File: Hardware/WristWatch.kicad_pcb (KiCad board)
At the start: 2 copper layers, 32 x 32 mm, 100 parts, among them J1 vcc, J2 gnd, J3 vcc, J4 gnd, Q1 Q_PMOS_GSD, U3 LIS2DE12, U4 AP2205-3.0, U5 MCP73832-2-OT, U6 ESP32-C3, Y2 40M, Y3 32.768k

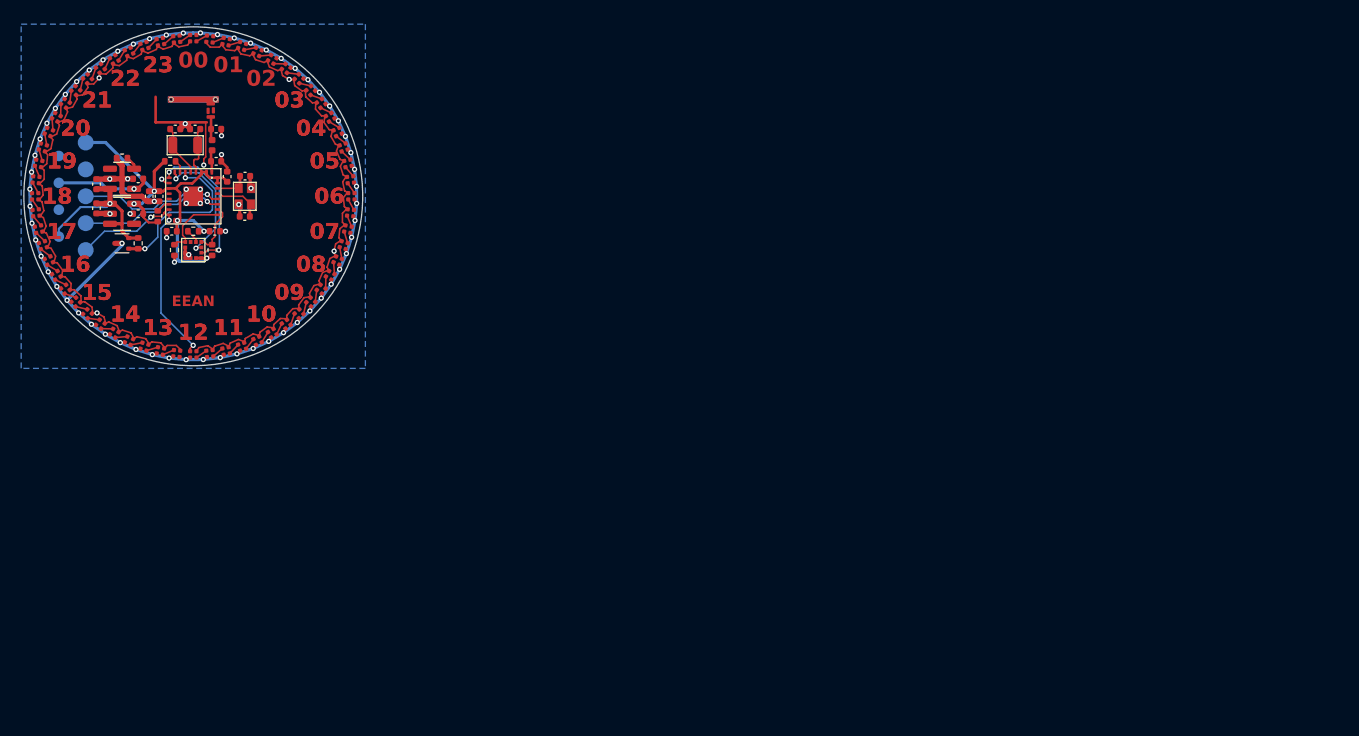
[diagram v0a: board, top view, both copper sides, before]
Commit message: rev C for shift registered discrete 0603 LEDs
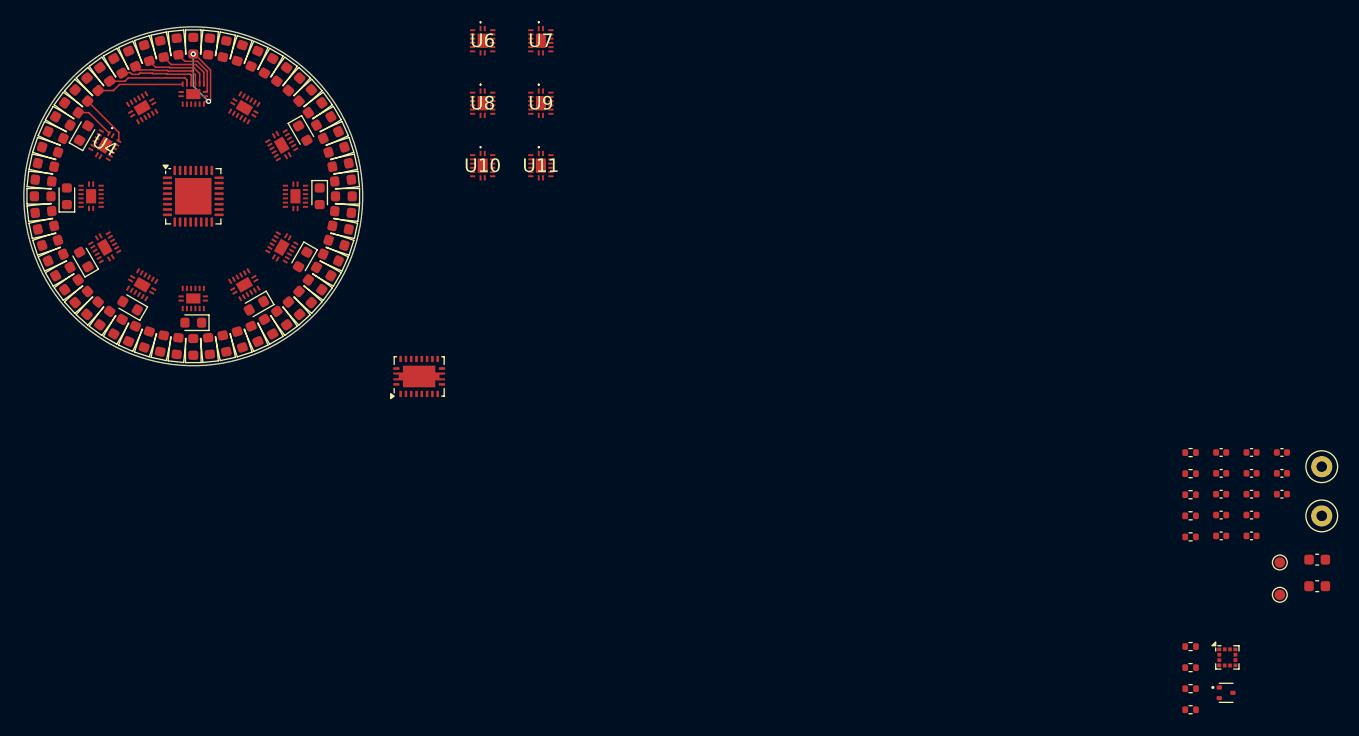
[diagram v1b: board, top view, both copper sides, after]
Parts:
- removed AE1: Antenna_Shield, Antenna_SMD:C209892
- removed C12: 1u, Capacitor_SMD:C_0402_1005Metric
- removed C13: 2u2, Capacitor_SMD:C_0402_1005Metric
- removed C15: 4u7, Capacitor_SMD:C_0402_1005Metric
- removed the C21 at (-2.03, 3.30)
- removed the C21 at (2.03, 3.30)
- removed J1, J3: vcc, TestPoint:TestPoint_Pad_D1.0mm
- removed J2, J4: gnd, TestPoint:TestPoint_Pad_D1.0mm
- removed L2: 3n, Inductor_SMD:L_0402_1005Metric
- removed TP3: BOOT, TestPoint:TestPoint_Pad_D1.5mm
- removed TP5: VCC, TestPoint:TestPoint_Pad_D1.5mm
- removed TP6: GND, TestPoint:TestPoint_Pad_D1.5mm
- removed Y2: 40M, Crystal:Crystal_SMD_2520-4Pin_2.5x2.0mm
- removed Y3: 32.768k, Crystal:Crystal_SMD_EuroQuartz_EQ161-2Pin_3.2x1.5mm
- added C2: 47n, Capacitor_SMD:C_0402_1005Metric, F.Cu at (97.1, 26.2)
- added C21: 10n, Capacitor_SMD:C_0402_1005Metric, F.Cu at (100.0, 32.1)
- added C23: 470n, Capacitor_SMD:C_0402_1005Metric, F.Cu at (102.8, 26.2)
- added C24: 22n, Capacitor_SMD:C_0402_1005Metric, F.Cu at (102.8, 28.1)
- added C25: 4.7u, Capacitor_SMD:C_0603_1608Metric, F.Cu at (106.2, 36.8)
- added D63: LED_Small, LED_SMD:LED_0603_1608Metric, F.Cu at (-10.3, -5.97)
- added D64: LED_Small, LED_SMD:LED_0603_1608Metric, F.Cu at (-11.9, 0.00)
- added D65: LED_Small, LED_SMD:LED_0603_1608Metric, F.Cu at (-10.3, 5.97)
- added D66: LED_Small, LED_SMD:LED_0603_1608Metric, F.Cu at (-5.97, 10.3)
- added D67: LED_Small, LED_SMD:LED_0603_1608Metric, F.Cu at (0.00, 11.9)
- added D68: LED_Small, LED_SMD:LED_0603_1608Metric, F.Cu at (5.97, 10.3)
- added D69: LED_Small, LED_SMD:LED_0603_1608Metric, F.Cu at (10.3, 5.97)
- added D70: LED_Small, LED_SMD:LED_0603_1608Metric, F.Cu at (11.9, 0.00)
- added D71: LED_Small, LED_SMD:LED_0603_1608Metric, F.Cu at (10.3, -5.97)
- added J5: vcc, TestPoint:TestPoint_Pad_D1.0mm, F.Cu at (102.6, 34.6)
- added J6: gnd, TestPoint:TestPoint_Pad_D1.0mm, F.Cu at (102.6, 37.6)
- added R11: 3k, Resistor_SMD:R_0402_1005Metric, F.Cu at (94.2, 28.2)
- added R13: 20K, Resistor_SMD:R_0402_1005Metric, F.Cu at (94.2, 32.2)
- added U1: 74HC595, KiCad:74HC595BZX, F.Cu at (4.83, -8.36)
- added U10: 74HC595, KiCad:74HC595BZX, F.Cu at (27.3, -2.89)
- added U11: 74HC595, KiCad:74HC595BZX, F.Cu at (32.8, -2.89)
- added U12: 74HC595, KiCad:74HC595BZX, F.Cu at (0.00, -9.65)
- added U13: 74HC595, KiCad:74HC595BZX, F.Cu at (-4.83, -8.36)
- added U15: 74HC595, KiCad:74HC595BZX, F.Cu at (-9.65, 0.00)
- added U16: 74HC595, KiCad:74HC595BZX, F.Cu at (-8.36, 4.83)
- added U17: 74HC595, KiCad:74HC595BZX, F.Cu at (-4.83, 8.36)
- added U18: 74HC595, KiCad:74HC595BZX, F.Cu at (0.00, 9.65)
- added U19: 74HC595, KiCad:74HC595BZX, F.Cu at (4.83, 8.36)
- added U2: STM32L412KBUx, Package_DFN_QFN:QFN-32-1EP_5x5mm_P0.5mm_EP3.45x3.45mm, F.Cu at (0.00, 0.00)
- added U20: 74HC595, KiCad:74HC595BZX, F.Cu at (8.36, 4.83)
- added U21: 74HC595, KiCad:74HC595BZX, F.Cu at (9.65, 0.00)
- added U22: 74HC595, KiCad:74HC595BZX, F.Cu at (8.36, -4.83)
- added U7: 74HC595, KiCad:74HC595BZX, F.Cu at (32.8, -14.7)
- added U8: 74HC595, KiCad:74HC595BZX, F.Cu at (27.3, -8.79)
- added U9: 74HC595, KiCad:74HC595BZX, F.Cu at (32.8, -8.79)
- C1: value 12p -> 68n
- C14: value 4u7 -> 100p
- C16: value 12p -> 470n
- C17: value 10u -> 100n
- C18: value 1.2p -> 4.7u; footprint Capacitor_SMD:C_0402_1005Metric -> Capacitor_SMD:C_0603_1608Metric
- C19: value 1.8p -> 22n
- C20: value 100n -> 10n
- C22: value 100n -> 22n
- C4: value 12p -> 39n
- C7: value 12p -> 2.2n
- D1, D10, D11, D12, D13, D14, D15, D16, D17, D18, D19, D2, D20, D21, D22, D23, D24, D25, D26, D27, D28, D29, D3, D30, D31, D32, D33, D34, D35, D36, D37, D38, D39, D4, D40, D41, D42, D43, D44, D45, D46, D47, D48, D49, D5, D50, D51, D52, D53, D54, D55, D56, D57, D58, D59, D6, D60, D7, D8, D9: value WS2812B -> LED_Small; footprint LED_Custom:XL-1010RGBC -> LED_SMD:LED_0603_1608Metric
- R1: value 100k -> 10K
- R10: value 10k -> 2.43K
- R12: value 100k -> 200
- TP1: value TX -> TestPoint; footprint TestPoint:TestPoint_Pad_D1.5mm -> TestPoint:TestPoint_Loop_D1.80mm_Drill1.0mm_Beaded; moved to F.Cu
- TP2: value RX -> TestPoint; footprint TestPoint:TestPoint_Pad_D1.5mm -> TestPoint:TestPoint_Loop_D1.80mm_Drill1.0mm_Beaded; moved to F.Cu
- U4: value AP2205-3.0 -> 74HC595; footprint Package_TO_SOT_SMD:SOT-23-5 -> KiCad:74HC595BZX
- U5: value MCP73832-2-OT -> BQ51050BRHL; footprint Package_TO_SOT_SMD:SOT-23-5 -> Package_DFN_QFN:Texas_VQFN-RHL-20
- U6: value ESP32-C3 -> 74HC595; footprint Package_DFN_QFN:QFN-32-1EP_5x5mm_P0.5mm_EP3.7x3.7mm -> KiCad:74HC595BZX
- moved TP2 120.0 mm to (106.6, 30.2)
- moved TP1 119.5 mm to (106.6, 25.5)
- moved Q1 112.6 mm to (97.6, 46.9), turned to 0 degrees
- moved C18 110.6 mm to (106.2, 34.3)
- moved C22 108.8 mm to (102.8, 24.2), turned to 0 degrees
- moved C14 107.7 mm to (97.1, 32.1), turned to 0 degrees
- moved C17 107.4 mm to (100.0, 26.2), turned to 0 degrees
- moved R6 106.5 mm to (94.2, 42.5), turned to 0 degrees
- moved R10 105.2 mm to (94.2, 26.2)
- moved U3 105.0 mm to (97.7, 43.6), turned to 0 degrees
- moved C4 104.6 mm to (97.1, 28.1), turned to 0 degrees
- moved R8 104.5 mm to (94.2, 46.5), turned to 0 degrees
- moved R9 104.5 mm to (94.2, 48.5), turned to 0 degrees
- moved C19 103.7 mm to (100.0, 28.1)
- moved R12 102.0 mm to (94.2, 30.2), turned to 0 degrees
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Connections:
- C1 pad 1: GND -> Net-(C1-Pad1)
- C1 pad 2: /xtl_ls+ -> /BMS/Coil+
- C14 pad 1: VBUS -> /BMS/Coil-
- C14 pad 2: GND -> /BMS/Coil+
- C16 pad 1: GND -> /BMS/Coil+
- C16 pad 2: /xtl_hs- -> Net-(U5-CLAMP1)
- C17 pad 1: +3V0 -> GND
- C17 pad 2: GND -> +BATT
- C18 pad 1: Net-(U6-LNA_IN) -> GND
- C18 pad 2: GND -> +BATT
- C19 pad 1: Net-(AE1-A) -> /BMS/Coil+
- C19 pad 2: GND -> Net-(U5-COMM1)
- C20 pad 1: GND -> /BMS/Coil+
- C20 pad 2: +3V0 -> Net-(U5-BOOT1)
- C22 pad 1: GND -> /BMS/Coil-
- C22 pad 2: +3V0 -> Net-(U5-COMM2)
- C4 pad 1: GND -> Net-(C1-Pad1)
- C4 pad 2: /xtl_ls- -> /BMS/Coil+
- C7 pad 1: GND -> /BMS/Coil-
- C7 pad 2: /xtl_hs+ -> /BMS/Coil+
- D1 pad 1: VLED -> /LED Array/LED_OUT
- D1 pad 2: Net-(D1-DOUT) -> Net-(D1-A)
- D10 pad 1: VLED -> /LED Array/LED_OUT
- D10 pad 2: Net-(D10-DOUT) -> Net-(D10-A)
- D11 pad 1: VLED -> /LED Array/LED_OUT
- D11 pad 2: Net-(D11-DOUT) -> Net-(D11-A)
- D12 pad 1: VLED -> /LED Array/LED_OUT
- D12 pad 2: Net-(D12-DOUT) -> Net-(D12-A)
- D13 pad 1: VLED -> /LED Array/LED_OUT
- D13 pad 2: Net-(D13-DOUT) -> Net-(D13-A)
- D14 pad 1: VLED -> /LED Array/LED_OUT
- D14 pad 2: Net-(D14-DOUT) -> Net-(D14-A)
- D15 pad 1: VLED -> /LED Array/LED_OUT
- D15 pad 2: Bank2 -> Net-(D15-A)
- D16 pad 1: VLED -> /LED Array/LED_OUT
- D16 pad 2: Net-(D16-DOUT) -> Net-(D16-A)
- D17 pad 1: VLED -> /LED Array/LED_OUT
- D17 pad 2: Net-(D17-DOUT) -> Net-(D17-A)
- D18 pad 1: VLED -> /LED Array/LED_OUT
- D18 pad 2: Net-(D18-DOUT) -> Net-(D18-A)
- D19 pad 1: VLED -> /LED Array/LED_OUT
- D19 pad 2: Net-(D19-DOUT) -> Net-(D19-A)
- D2 pad 1: VLED -> /LED Array/LED_OUT
- D2 pad 2: Net-(D2-DOUT) -> Net-(D2-A)
- D20 pad 1: VLED -> /LED Array/LED_OUT
- D20 pad 2: Net-(D20-DOUT) -> Net-(D20-A)
- D21 pad 1: VLED -> /LED Array/LED_OUT
- D21 pad 2: Net-(D21-DOUT) -> Net-(D21-A)
- D22 pad 1: VLED -> /LED Array/LED_OUT
- D22 pad 2: Net-(D22-DOUT) -> Net-(D22-A)
- D23 pad 1: VLED -> /LED Array/LED_OUT
- D23 pad 2: Net-(D23-DOUT) -> Net-(D23-A)
- D24 pad 1: VLED -> /LED Array/LED_OUT
- D24 pad 2: Net-(D24-DOUT) -> Net-(D24-A)
- D25 pad 1: VLED -> /LED Array/LED_OUT
- D25 pad 2: Net-(D25-DOUT) -> Net-(D25-A)
- D26 pad 1: VLED -> /LED Array/LED_OUT
- D26 pad 2: Net-(D26-DOUT) -> Net-(D26-A)
- D27 pad 1: VLED -> /LED Array/LED_OUT
- D27 pad 2: Net-(D27-DOUT) -> Net-(D27-A)
- D28 pad 1: VLED -> /LED Array/LED_OUT
- D28 pad 2: Net-(D28-DOUT) -> Net-(D28-A)
- D29 pad 1: VLED -> /LED Array/LED_OUT
- D29 pad 2: Net-(D29-DOUT) -> Net-(D29-A)
- D3 pad 1: VLED -> /LED Array/LED_OUT
- D3 pad 2: Net-(D3-DOUT) -> Net-(D3-A)
- D30 pad 1: VLED -> /LED Array/LED_OUT
- D30 pad 2: unconnected-(D30-DOUT-Pad2) -> Net-(D30-A)
- D31 pad 1: VLED -> /LED Array/LED_OUT
- D31 pad 2: Net-(D31-DOUT) -> Net-(D31-A)
- D32 pad 1: VLED -> /LED Array/LED_OUT
- D32 pad 2: Net-(D32-DOUT) -> Net-(D32-A)
- D33 pad 1: VLED -> /LED Array/LED_OUT
- D33 pad 2: Net-(D33-DOUT) -> Net-(D33-A)
- D34 pad 1: VLED -> /LED Array/LED_OUT
- D34 pad 2: Net-(D34-DOUT) -> Net-(D34-A)
- D35 pad 1: VLED -> /LED Array/LED_OUT
- D35 pad 2: Net-(D35-DOUT) -> Net-(D35-A)
- D36 pad 1: VLED -> /LED Array/LED_OUT
- D36 pad 2: Net-(D36-DOUT) -> Net-(D36-A)
- D37 pad 1: VLED -> /LED Array/LED_OUT
- D37 pad 2: Net-(D37-DOUT) -> Net-(D37-A)
- D38 pad 1: VLED -> /LED Array/LED_OUT
- D38 pad 2: Net-(D38-DOUT) -> Net-(D38-A)
- D39 pad 1: VLED -> /LED Array/LED_OUT
- D39 pad 2: Net-(D39-DOUT) -> Net-(D39-A)
- D4 pad 1: VLED -> /LED Array/LED_OUT
- D4 pad 2: Net-(D4-DOUT) -> Net-(D4-A)
- D40 pad 1: VLED -> /LED Array/LED_OUT
- D40 pad 2: Net-(D40-DOUT) -> Net-(D40-A)
- D41 pad 1: VLED -> /LED Array/LED_OUT
- D41 pad 2: Net-(D41-DOUT) -> Net-(D41-A)
- D42 pad 1: VLED -> /LED Array/LED_OUT
- D42 pad 2: Net-(D42-DOUT) -> Net-(D42-A)
- D43 pad 1: VLED -> /LED Array/LED_OUT
- D43 pad 2: Net-(D43-DOUT) -> Net-(D43-A)
- D44 pad 1: VLED -> /LED Array/LED_OUT
- D44 pad 2: Net-(D44-DOUT) -> Net-(D44-A)
- D45 pad 1: VLED -> /LED Array/LED_OUT
- D45 pad 2: Bank3 -> Net-(D45-A)
- D46 pad 1: VLED -> /LED Array/LED_OUT
- D46 pad 2: Net-(D46-DOUT) -> Net-(D46-A)
- D47 pad 1: VLED -> /LED Array/LED_OUT
- D47 pad 2: Net-(D47-DOUT) -> Net-(D47-A)
- D48 pad 1: VLED -> /LED Array/LED_OUT
- D48 pad 2: Net-(D48-DOUT) -> Net-(D48-A)
- D49 pad 1: VLED -> /LED Array/LED_OUT
- D49 pad 2: Net-(D49-DOUT) -> Net-(D49-A)
- D5 pad 1: VLED -> /LED Array/LED_OUT
- D5 pad 2: Net-(D5-DOUT) -> Net-(D5-A)
- D50 pad 1: VLED -> /LED Array/LED_OUT
- D50 pad 2: Net-(D50-DOUT) -> Net-(D50-A)
- D51 pad 1: VLED -> /LED Array/LED_OUT
- D51 pad 2: Net-(D51-DOUT) -> Net-(D51-A)
- D52 pad 1: VLED -> /LED Array/LED_OUT
- D52 pad 2: Net-(D52-DOUT) -> Net-(D52-A)
- D53 pad 1: VLED -> /LED Array/LED_OUT
- D53 pad 2: Net-(D53-DOUT) -> Net-(D53-A)
- D54 pad 1: VLED -> /LED Array/LED_OUT
- D54 pad 2: Net-(D54-DOUT) -> Net-(D54-A)
- D55 pad 1: VLED -> /LED Array/LED_OUT
- D55 pad 2: Net-(D55-DOUT) -> Net-(D55-A)
- D56 pad 1: VLED -> /LED Array/LED_OUT
- D56 pad 2: Net-(D56-DOUT) -> Net-(D56-A)
- D57 pad 1: VLED -> /LED Array/LED_OUT
- D57 pad 2: Net-(D57-DOUT) -> Net-(D57-A)
- D58 pad 1: VLED -> /LED Array/LED_OUT
- D58 pad 2: Net-(D58-DOUT) -> Net-(D58-A)
- D59 pad 1: VLED -> /LED Array/LED_OUT
- D59 pad 2: Net-(D59-DOUT) -> Net-(D59-A)
- D6 pad 1: VLED -> /LED Array/LED_OUT
- D6 pad 2: Net-(D6-DOUT) -> Net-(D6-A)
- D60 pad 1: VLED -> /LED Array/LED_OUT
- D60 pad 2: Bank1 -> Net-(D100-A)
- D7 pad 1: VLED -> /LED Array/LED_OUT
- D7 pad 2: Net-(D7-DOUT) -> Net-(D7-A)
- D8 pad 1: VLED -> /LED Array/LED_OUT
- D8 pad 2: Net-(D8-DOUT) -> Net-(D8-A)
- D9 pad 1: VLED -> /LED Array/LED_OUT
- D9 pad 2: Net-(D10-DIN) -> Net-(D9-A)
- R1 pad 1: Net-(U6-GPIO8) -> Net-(U5-TS/CTRL)
- R1 pad 2: +3V0 -> GND
- R10 pad 1: GND -> Net-(U5-TERM)
- R10 pad 2: Net-(U5-PROG) -> GND
- R12 pad 1: Net-(U6-CHIP_EN) -> FOD
- R12 pad 2: +3V0 -> GND
- TP1 pad 1: ESP_TX -> Net-(C1-Pad1)
- TP2 pad 1: ESP_RX -> /BMS/Coil-
- U4 pad 1: +BATT -> Net-(D10-A)
- U4 pad 2: GND -> Net-(D11-A)
- U4 pad 3: +BATT -> Net-(D12-A)
- U4 pad 4: unconnected-(U4-NC-Pad4) -> Net-(D13-A)
- U4 pad 5: +3V0 -> Net-(D14-A)
- U5 pad 1: BMS_STATUS -> GND
- U5 pad 2: GND -> /BMS/Coil+
- U5 pad 3: +BATT -> Net-(U5-BOOT1)
- U5 pad 4: VBUS -> +BATT
- U5 pad 5: Net-(U5-PROG) -> Net-(U5-CLAMP1)
- U6 pad 1: Net-(U6-LNA_IN) -> Net-(D18-A)
- U6 pad 10: unconnected-(U6-MTDI-Pad10) -> /LED Array/SR_CLEAR_IN
- U6 pad 11: +3V0 -> /LED Array/SR_SERIAL_IN
- U6 pad 12: unconnected-(U6-MTCK-Pad12) -> /LED Array/SR_LATCH_IN
- U6 pad 13: BMS_STATUS -> /LED Array/SR_OE_IN
- U6 pad 14: Net-(U6-GPIO8) -> Net-(U4-QH')
- U6 pad 15: ESP_BOOT -> Net-(D17-A)
- U6 pad 16: LED_DATA -> VLED
- U6 pad 17: +3V0 -> (no net)
- U6 pad 2: +3V0 -> Net-(D19-A)
- U6 pad 3: +3V0 -> Net-(D20-A)
- U6 pad 4: /xtl_ls+ -> Net-(D21-A)
- U6 pad 5: /xtl_ls- -> Net-(D22-A)
- U6 pad 6: LED_PWR_EN -> Net-(D23-A)
- U6 pad 7: Net-(U6-CHIP_EN) -> Net-(D24-A)
- U6 pad 8: IMU_MOVE_INT -> GND
- U6 pad 9: IMU_SPAR_INT -> Net-(U6-QH')
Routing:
- net GND: track 146.1 -> 0.00 mm, vias 22 -> 0
- net VLED: track 130.7 -> 0.00 mm, vias 61 -> 0
- net +3V0: track 46.8 -> 0.00 mm, vias 6 -> 0
- net +BATT: track 17.1 -> 0.00 mm, vias 1 -> 0
- net LED_PWR_EN: track 15.6 -> 0.00 mm, vias 2 -> 0
- net LED_DATA: track 14.6 -> 0.00 mm, vias 2 -> 0
- net IMU_SPAR_INT: track 13.9 -> 0.00 mm, vias 2 -> 0
- net ESP_TX: track 13.7 -> 0.00 mm, vias 1 -> 0
- net ESP_RX: track 13.7 -> 0.00 mm, vias 1 -> 0
- net IMU_MOVE_INT: track 12.2 -> 0.00 mm, vias 2 -> 0
- net Net-(D1-A): track 0.00 -> 11.0 mm, vias 0 -> 2
- net ESP_BOOT: track 9.52 -> 0.00 mm, vias 1 -> 0
- net VBUS: track 8.86 -> 0.00 mm, vias 1 -> 0
- net Net-(D8-A): track 0.00 -> 8.25 mm
- net Net-(D7-A): track 0.00 -> 7.90 mm
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- removed copper zone on B.Cu, net GND
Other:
- board text removed: "00"
- board text removed: "01"
- board text removed: "02"
- board text removed: "03"
- board text removed: "04"
- board text removed: "05"
- board text removed: "06"
- board text removed: "07"
- board text removed: "08"
- board text removed: "09"
- board text removed: "10"
- board text removed: "11"
- board text removed: "12"
- board text removed: "13"
- board text removed: "14"
- board text removed: "15"
- board text removed: "16"
- board text removed: "17"
- board text removed: "18"
- board text removed: "19"
- board text removed: "20"
- board text removed: "21"
- board text removed: "22"
- board text removed: "23"
- board text removed: "EEAN"

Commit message: semi-final component placements and final component selections. Abandoning due to high routing complexity and need for a 4L board.
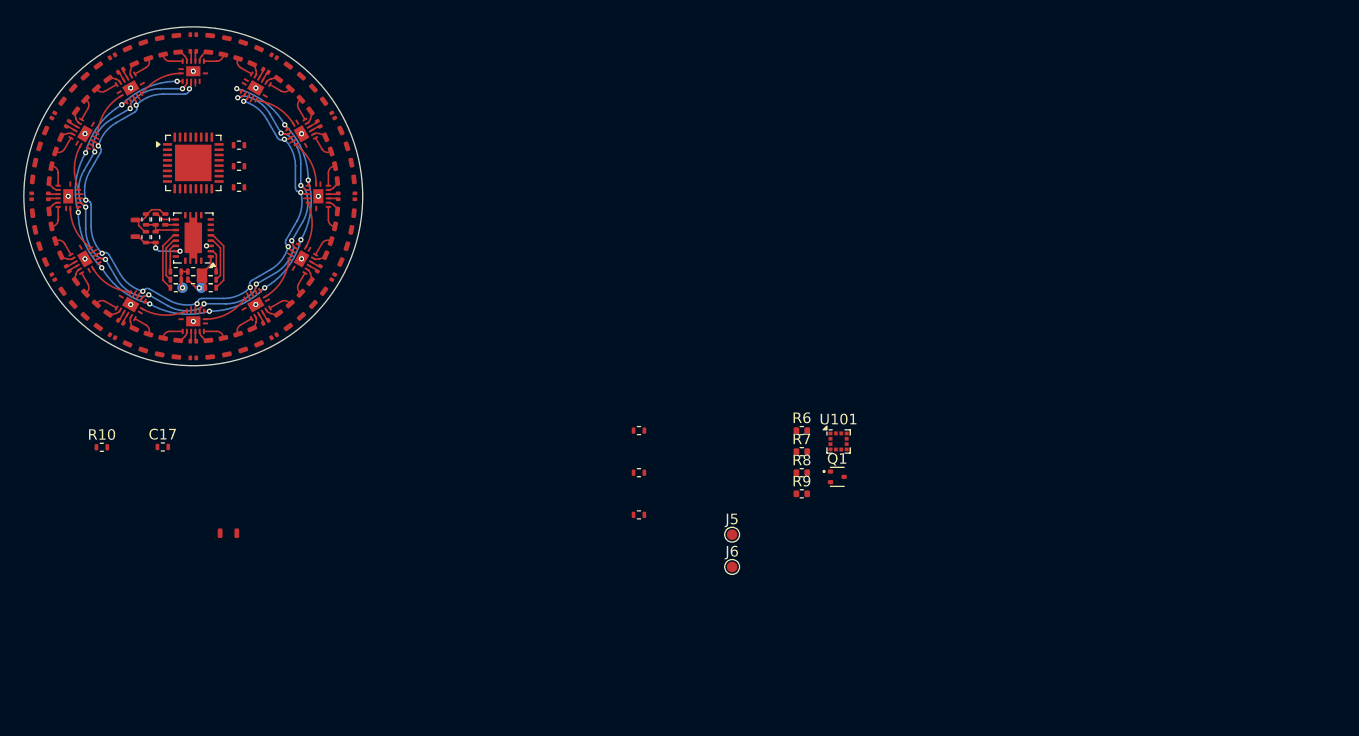
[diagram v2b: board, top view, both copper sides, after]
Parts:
- removed D63, D64, D65, D66, D67, D68, D69, D70, D71: LED_Small, LED_SMD:LED_0603_1608Metric
- removed U13, U15, U16, U17, U18, U19, U20, U21, U22: 74HC595, KiCad:74HC595BZX
- added C3: 100n, LED_Custom:SMD_0402-2, F.Cu at (4.32, -4.83)
- added C5: 100n, LED_Custom:SMD_0402-2, F.Cu at (4.32, -2.84)
- added C6: 100n, LED_Custom:SMD_0402-2, F.Cu at (4.32, -0.85)
- added U100: STM32L412KBUx, Package_DFN_QFN:QFN-32-1EP_5x5mm_P0.5mm_EP3.45x3.45mm, F.Cu at (0.00, -3.15)
- added U101: LIS2DE12, Package_LGA:LGA-12_2x2mm_P0.5mm, F.Cu at (61.0, 23.2)
- added U102: BQ51050BRHL, Package_DFN_QFN:Texas_VQFN-RHL-20, F.Cu at (0.00, 3.94)
- C1, C14, C16, C17, C19, C20, C21, C22, C23, C24, C4, C7: footprint Capacitor_SMD:C_0402_1005Metric -> LED_Custom:SMD_0402-2
- C18, C25: footprint Capacitor_SMD:C_0603_1608Metric -> LED_Custom:LED_0603-2
- C2: value 47n -> 220n; footprint Capacitor_SMD:C_0402_1005Metric -> LED_Custom:SMD_0402-2
- D1, D10, D11, D12, D14, D15, D16, D17, D19, D2, D20, D21, D22, D24, D25, D26, D27, D29, D30, D31, D32, D34, D35, D36, D37, D39, D4, D40, D41, D42, D44, D45, D46, D47, D49, D5, D50, D51, D52, D54, D55, D56, D57, D59, D6, D60, D7, D9: footprint LED_SMD:LED_0603_1608Metric -> LED_Custom:LED_0603-2
- D13, D18, D23, D28, D3, D33, D38, D43, D48, D53, D58, D8: footprint LED_SMD:LED_0603_1608Metric -> LED_Custom:LED_0603-4
- R1, R10, R11, R12, R13: footprint Resistor_SMD:R_0402_1005Metric -> LED_Custom:SMD_0402-2
- TP1, TP2: footprint TestPoint:TestPoint_Loop_D1.80mm_Drill1.0mm_Beaded -> TestPoint:TestPoint_Pad_D1.0mm; moved to B.Cu
- U1: value 74HC595 -> 74HC595BZX
- U2: value STM32L412KBUx -> 74HC595; footprint Package_DFN_QFN:QFN-32-1EP_5x5mm_P0.5mm_EP3.45x3.45mm -> KiCad:74HC595BZX
- U3: value LIS2DE12 -> 74HC595; footprint Package_LGA:LGA-12_2x2mm_P0.5mm -> KiCad:74HC595BZX
- U5: value BQ51050BRHL -> 74HC595; footprint Package_DFN_QFN:Texas_VQFN-RHL-20 -> KiCad:74HC595BZX
- moved U3 118.7 mm to (-10.2, -5.91), turned to -30 degrees
- moved C25 116.6 mm to (-5.46, 3.02), turned to -90 degrees
- moved C24 110.0 mm to (-4.47, 3.86), turned to -90 degrees
- moved TP2 109.7 mm to (-1.02, 8.64)
- moved TP1 107.2 mm to (0.76, 8.64)
- moved C23 106.1 mm to (-1.65, 7.87), turned to 180 degrees
- moved C22 105.6 mm to (-1.65, 8.64), turned to 180 degrees
- moved C21 104.6 mm to (-1.65, 7.11), turned to 180 degrees
- moved C18 102.9 mm to (3.33, 31.8)
- moved C17 102.9 mm to (-2.87, 23.7)
- moved R10 102.9 mm to (-8.63, 23.7)
- moved R12 102.6 mm to (-4.47, 2.18), turned to 90 degrees
- moved R13 101.8 mm to (-3.56, 3.86), turned to -90 degrees
- moved R11 101.2 mm to (-3.56, 2.18), turned to 90 degrees
- moved C20 101.0 mm to (1.65, 7.11)
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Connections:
- C16 pad 2: Net-(U5-CLAMP1) -> Net-(U102-CLAMP1)
- C19 pad 2: Net-(U5-COMM1) -> Net-(U102-COMM1)
- C2 pad 1: Net-(C1-Pad1) -> Net-(C2-Pad1)
- C20 pad 2: Net-(U5-BOOT1) -> Net-(U102-BOOT1)
- C21 pad 2: Net-(U5-BOOT2) -> Net-(U102-BOOT2)
- C22 pad 2: Net-(U5-COMM2) -> Net-(U102-COMM2)
- C23 pad 2: Net-(U5-CLAMP2) -> Net-(U102-CLAMP2)
- D13 pad 2: Net-(D13-A) -> /LED Array/LED_OUT
- D18 pad 2: Net-(D18-A) -> /LED Array/LED_OUT
- D23 pad 2: Net-(D23-A) -> /LED Array/LED_OUT
- D28 pad 2: Net-(D28-A) -> /LED Array/LED_OUT
- D3 pad 2: Net-(D3-A) -> /LED Array/LED_OUT
- D33 pad 2: Net-(D33-A) -> /LED Array/LED_OUT
- D38 pad 2: Net-(D38-A) -> /LED Array/LED_OUT
- D43 pad 2: Net-(D43-A) -> /LED Array/LED_OUT
- D48 pad 2: Net-(D48-A) -> /LED Array/LED_OUT
- D53 pad 2: Net-(D53-A) -> /LED Array/LED_OUT
- D58 pad 2: Net-(D58-A) -> /LED Array/LED_OUT
- D60 pad 2: Net-(D100-A) -> Net-(D60-A)
- D8 pad 2: Net-(D8-A) -> /LED Array/LED_OUT
- R1 pad 1: Net-(U5-TS/CTRL) -> Net-(U102-TS/CTRL)
- R10 pad 1: Net-(U5-TERM) -> Net-(U102-TERM)
- R9 pad 2: Net-(U3-~{CS}) -> Net-(U101-~{CS})
- TP1 pad 1: Net-(C1-Pad1) -> Net-(C2-Pad1)
- U1 pad 17: (no net) -> GND
- U1 pad 2: Net-(D3-A) -> Net-(D1-A)
- U1 pad 3: Net-(D4-A) -> Net-(D2-A)
- U1 pad 4: Net-(D5-A) -> Net-(U1-QE)
- U1 pad 5: Net-(D6-A) -> Net-(U1-QF)
- U1 pad 6: Net-(D7-A) -> Net-(D4-A)
- U1 pad 7: Net-(D8-A) -> Net-(D5-A)
- U10 pad 17: (no net) -> GND
- U10 pad 2: Net-(D51-A) -> Net-(D46-A)
- U10 pad 3: Net-(D52-A) -> Net-(D47-A)
- U10 pad 4: Net-(D53-A) -> Net-(U10-QE)
- U10 pad 5: Net-(D54-A) -> Net-(U10-QF)
- U10 pad 6: Net-(D55-A) -> Net-(D49-A)
- U10 pad 7: Net-(D56-A) -> Net-(D50-A)
- U11 pad 17: (no net) -> GND
- U11 pad 2: Net-(D59-A) -> Net-(D51-A)
- U11 pad 3: Net-(D100-A) -> Net-(D52-A)
- U11 pad 4: unconnected-(U11-QE-Pad4) -> Net-(U11-QE)
- U11 pad 5: unconnected-(U11-QF-Pad5) -> Net-(U11-QF)
- U11 pad 6: unconnected-(U11-QG-Pad6) -> Net-(D54-A)
- U11 pad 7: unconnected-(U11-QH-Pad7) -> Net-(D55-A)
- U11 pad 9: unconnected-(U11-QH'-Pad9) -> Net-(U11-QH')
- U12 pad 14: /LED Array/SR_SER_IN -> Net-(U11-QH')
- U12 pad 17: (no net) -> GND
- U12 pad 2: Net-(D3-A) -> Net-(D56-A)
- U12 pad 3: Net-(D4-A) -> Net-(D57-A)
- U12 pad 4: Net-(D5-A) -> Net-(U12-QE)
- U12 pad 5: Net-(D6-A) -> Net-(U12-QF)
- U12 pad 6: Net-(D7-A) -> Net-(D59-A)
- U12 pad 7: Net-(D8-A) -> Net-(D60-A)
- U12 pad 9: Net-(U1-QH') -> unconnected-(U12-QH&apos;-Pad9)
- U2 pad 10: unconnected-(U2-PA4-Pad10) -> /LED Array/SR_CLEAR_IN
- U2 pad 11: unconnected-(U2-PA5-Pad11) -> /LED Array/SR_SERIAL_IN
- U2 pad 12: unconnected-(U2-PA6-Pad12) -> /LED Array/SR_LATCH_IN
- U2 pad 13: unconnected-(U2-PA7-Pad13) -> /LED Array/SR_OE_IN
- U2 pad 14: unconnected-(U2-PB0-Pad14) -> Net-(U1-QH')
- U2 pad 16: GND -> VLED
- U2 pad 17: +3V0 -> GND
- U2 pad 2: unconnected-(U2-PC14-Pad2) -> Net-(D6-A)
- U2 pad 3: unconnected-(U2-PC15-Pad3) -> Net-(D7-A)
- U2 pad 4: unconnected-(U2-NRST-Pad4) -> Net-(U2-QE)
- U2 pad 5: +3V0 -> Net-(U2-QF)
- U2 pad 6: unconnected-(U2-PA0-Pad6) -> Net-(D9-A)
- U2 pad 7: unconnected-(U2-PA1-Pad7) -> Net-(D10-A)
- U2 pad 8: unconnected-(U2-PA2-Pad8) -> GND
- U2 pad 9: unconnected-(U2-PA3-Pad9) -> Net-(U2-QH')
- U3 pad 10: +3V0 -> /LED Array/SR_CLEAR_IN
- U3 pad 11: IMU_SPAR_INT -> /LED Array/SR_SERIAL_IN
- U3 pad 12: IMU_MOVE_INT -> /LED Array/SR_LATCH_IN
- U3 pad 2: Net-(U3-~{CS}) -> Net-(D11-A)
- U3 pad 3: unconnected-(U3-SA0/SDO-Pad3) -> Net-(D12-A)
- U3 pad 4: SDA -> Net-(U3-QE)
- U3 pad 5: GND -> Net-(U3-QF)
- U3 pad 6: GND -> Net-(D14-A)
- U3 pad 7: GND -> Net-(D15-A)
- U3 pad 9: +3V0 -> Net-(U3-QH')
- U4 pad 14: Net-(U1-QH') -> Net-(U3-QH')
- U4 pad 17: (no net) -> GND
- U4 pad 2: Net-(D11-A) -> Net-(D16-A)
- U4 pad 3: Net-(D12-A) -> Net-(D17-A)
- U4 pad 4: Net-(D13-A) -> Net-(U4-QE)
- U4 pad 5: Net-(D14-A) -> Net-(U4-QF)
- U4 pad 6: Net-(D15-A) -> Net-(D19-A)
- U4 pad 7: Net-(D16-A) -> Net-(D20-A)
- U5 pad 10: Net-(U5-TERM) -> /LED Array/SR_CLEAR_IN
- U5 pad 11: GND -> /LED Array/SR_SERIAL_IN
- U5 pad 12: ILIM -> /LED Array/SR_LATCH_IN
- U5 pad 13: Net-(U5-TS/CTRL) -> /LED Array/SR_OE_IN
- U5 pad 14: FOD -> Net-(U4-QH')
- U5 pad 16: Net-(U5-CLAMP2) -> VLED
- U5 pad 17: Net-(U5-BOOT2) -> GND
- U5 pad 2: /BMS/Coil+ -> Net-(D21-A)
- U5 pad 3: Net-(U5-BOOT1) -> Net-(D22-A)
- U5 pad 4: +BATT -> Net-(U5-QE)
- U5 pad 5: Net-(U5-CLAMP1) -> Net-(U5-QF)
- U5 pad 6: Net-(U5-COMM1) -> Net-(D24-A)
- U5 pad 7: /BMS/~{CHG} -> Net-(D25-A)
- U5 pad 8: unconnected-(U5-~{AD-EN}-Pad8) -> GND
- U5 pad 9: GND -> Net-(U5-QH')
- U6 pad 14: Net-(U4-QH') -> Net-(U5-QH')
- U6 pad 17: (no net) -> GND
- U6 pad 2: Net-(D19-A) -> Net-(D26-A)
- U6 pad 3: Net-(D20-A) -> Net-(D27-A)
- U6 pad 4: Net-(D21-A) -> Net-(U6-QE)
- U6 pad 5: Net-(D22-A) -> Net-(U6-QF)
- U6 pad 6: Net-(D23-A) -> Net-(D29-A)
- U6 pad 7: Net-(D24-A) -> Net-(D30-A)
- U7 pad 17: (no net) -> GND
- U7 pad 2: Net-(D27-A) -> Net-(D31-A)
- U7 pad 3: Net-(D28-A) -> Net-(D32-A)
- U7 pad 4: Net-(D29-A) -> Net-(U7-QE)
- U7 pad 5: Net-(D30-A) -> Net-(U7-QF)
- U7 pad 6: Net-(D31-A) -> Net-(D34-A)
- U7 pad 7: Net-(D32-A) -> Net-(D35-A)
- U8 pad 17: (no net) -> GND
- U8 pad 2: Net-(D35-A) -> Net-(D36-A)
- U8 pad 3: Net-(D36-A) -> Net-(D37-A)
- U8 pad 4: Net-(D37-A) -> Net-(U8-QE)
- U8 pad 5: Net-(D38-A) -> Net-(U8-QF)
- U9 pad 17: (no net) -> GND
- U9 pad 2: Net-(D43-A) -> Net-(D41-A)
- U9 pad 3: Net-(D44-A) -> Net-(D42-A)
- U9 pad 4: Net-(D45-A) -> Net-(U9-QE)
- U9 pad 5: Net-(D46-A) -> Net-(U9-QF)
- U9 pad 6: Net-(D47-A) -> Net-(D44-A)
- U9 pad 7: Net-(D48-A) -> Net-(D45-A)
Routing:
- net /LED Array/SR_SERIAL_IN: track 0.00 -> 73.6 mm, vias 0 -> 12
- net /LED Array/SR_LATCH_IN: track 0.00 -> 70.2 mm, vias 0 -> 12
- net /LED Array/SR_CLEAR_IN: track 0.00 -> 70.0 mm, vias 0 -> 12
- net Net-(D1-A): track 11.0 -> 2.19 mm, vias 2 -> 0
- net Net-(D8-A): track 8.25 -> 0.00 mm
- net Net-(D7-A): track 7.90 -> 1.02 mm
- net Net-(U102-COMM1): track 0.00 -> 5.88 mm
- net Net-(U102-COMM2): track 0.00 -> 5.88 mm
- net GND: track 0.00 -> 5.73 mm, vias 0 -> 12
- net Net-(D3-A): track 5.49 -> 0.00 mm
- net RECT: track 0.00 -> 5.48 mm, vias 0 -> 2
- net Net-(D6-A): track 7.58 -> 2.18 mm
- net /LED Array/SR_OE_IN: track 0.00 -> 5.35 mm
- net Net-(D4-A): track 6.23 -> 1.02 mm
- net Net-(D5-A): track 6.87 -> 2.19 mm
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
